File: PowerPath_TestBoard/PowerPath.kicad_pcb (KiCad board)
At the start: 2 copper layers, 86 parts, among them J1 24V Test, J2 +24V_Ext, J3 12V Test, J4 5V Test, J5 3V Test, J6 +V_in_24V, J7 GND, J8 +Vin_5V, U1 LM76202QPWPRQ1, U2 MCP1826S_LDO, U3 LMR51635XDDCR, U4 LMR51635XDDCR

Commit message: 1st iteration layout review
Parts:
- removed TP13: V_in_24V, TestPoint:TestPoint_THTPad_D3.0mm_Drill1.5mm
- added J9: +3V3_Ext, UTSVT_Connectors:5754, F.Cu at (161.7, 71.5)
- F1: value 1A -> 5A
- JP1, JP2, JP3, JP4, JP5, JP6, JP7: footprint Connector_PinHeader_1.00mm:PinHeader_1x02_P1.00mm_Vertical -> Connector_PinHeader_2.54mm:PinHeader_1x02_P2.54mm_Vertical
- moved TP9 194.2 mm to (224.3, 77.1)
- moved J4 180.0 mm to (224.6, 102.0)
- moved TP8 163.4 mm to (215.7, 117.3)
- moved J6 159.3 mm to (224.4, 88.0)
- moved TP16 155.4 mm to (214.2, 102.2)
- moved TP15 153.9 mm to (207.1, 96.2)
- moved TP14 149.7 mm to (214.1, 96.1)
- moved TP7 148.0 mm to (207.1, 101.9)
- moved J8 147.1 mm to (224.5, 114.7)
- moved R7 143.2 mm to (213.8, 110.6), turned to -90 degrees
- moved R18 136.2 mm to (182.1, 96.5), turned to 90 degrees
- moved TP3 134.9 mm to (179.1, 69.2)
- moved C14 133.1 mm to (197.5, 97.5)
- moved R8 132.2 mm to (197.2, 113.6), turned to -90 degrees
- moved R19 131.9 mm to (185.1, 96.5), turned to -90 degrees
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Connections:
- net +24V_Ext renamed /+24V_Ext
- net +Vin_5V renamed /+Vin_5V
- net Net-(J2-Pin_1) renamed /+24V_Ext_In
- C12 pad 1: +V_in_24V -> /+V_in_24V
- C8 pad 1: /12VBuck/V_in_24V -> /+V_in_24V
- J6 pad 1: +V_in_24V -> /+V_in_24V
- JP5 pad 2: /12VBuck/V_in_24V -> /+V_in_24V
- JP6 pad 2: +V_in_24V -> /+V_in_24V
- R3 pad 1: /12VBuck/V_in_24V -> /+V_in_24V
- R4 pad 1: +V_in_24V -> /+V_in_24V
- TP9 pad 1: /12VBuck/V_in_24V -> /+V_in_24V
- U3 pad 2: /12VBuck/V_in_24V -> /+V_in_24V
- U3 pad 3: /12VBuck/V_in_24V -> /+V_in_24V
- U4 pad 2: +V_in_24V -> /+V_in_24V
- U4 pad 3: +V_in_24V -> /+V_in_24V
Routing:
- net Net-(D7-A): track 0.00 -> 77.5 mm, vias 0 -> 2
- net Net-(D2-A): track 0.00 -> 68.1 mm, vias 0 -> 2
- net Net-(D8-A): track 0.00 -> 67.9 mm, vias 0 -> 2
- net Net-(D6-A): track 0.00 -> 60.1 mm, vias 0 -> 2
- net Net-(D4-A): track 0.00 -> 48.5 mm, vias 0 -> 2
- net Net-(D3-A): track 0.00 -> 48.5 mm, vias 0 -> 2
- net /+V_in_24V: track 0.00 -> 46.6 mm
- net /12VBuck/FB: track 0.00 -> 41.2 mm
- net /5VBuck/SW: track 0.00 -> 37.3 mm, vias 0 -> 1
- net Net-(D1-A): track 0.00 -> 35.5 mm, vias 0 -> 2
- net /5VBuck/CB: track 0.00 -> 27.5 mm, vias 0 -> 1
- net /Fault_TP: track 0.00 -> 26.9 mm
- net Net-(D5-A): track 0.00 -> 25.3 mm, vias 0 -> 2
- net /V_out_12V: track 0.00 -> 25.3 mm
- net /5VBuck/FB: track 0.00 -> 22.9 mm
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- added copper zone on F.Cu, net /+24V_Ext
- added copper zone on F.Cu, net /+24V_Ext_In
- added copper zone on F.Cu, net /+V_in_24V
- added copper zone on F.Cu, net /+V_out_5V_Buck
- added copper zone on F.Cu, net /+Vin_5V
- added copper zone on F.Cu, net /+Vout_3V3
- added copper zone on F.Cu, net /24V_OUT
- added copper zone on F.Cu, net /PowerProtection/RTN
- added copper zone on F.Cu, net /V_out_12V
- added copper zone on B.Cu, net GND
- added copper zone on F.Cu, net GND
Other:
- board outline added: 95.5 x 62.9 mm
- board text added: "+24V Ext"
- board text added: "+3V3 Ext"
- board text added: "+5V Ext"
- board text added: "12V Buck TP"
- board text added: "5V Buck TP"
- board text added: "5V Vout"
- board text added: "CB"
- board text added: "FB"
- board text added: "PP-12V"
- board text added: "PP-5V"
- board text added: "Power Path Test Board"
- board text added: "SW"
- board text removed: "+24V PP"
- board text removed: "+5V"
- board text removed: "12V Buck CB"
- board text removed: "12V Buck FB"
- board text removed: "12V Buck SW"
- board text removed: "5V Buck CB"
- board text removed: "5V Buck FB"
- board text removed: "5V Buck SW"
- board text removed: "PP-12V Buck"
- board text removed: "PP-5V Buck"
- board text removed: "U3"
- board text removed: "U4"
- board text removed: "Vin_24V"
- board text removed: "Vout 5V"

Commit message: addressed all final comments, review?
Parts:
- removed the C1 at (165.6, 79.9)
- removed the C2 at (168.5, 80.2)
- removed the D9 at (162.4, 87.3)
- removed the J9 at (161.7, 71.5)
- removed the R16 at (184.4, 84.1)
- removed the R17 at (167.9, 89.9)
- removed the TP2 at (171.8, 69.0)
- removed the TP3 at (179.1, 69.2)
- removed the U1 at (174.7, 82.8)
- added C6: 10n, Capacitor_SMD:C_0603_1608Metric_Pad1.08x0.95mm_HandSolder, F.Cu at (171.5, 77.5)
- added C7: 10u, Capacitor_SMD:C_0805_2012Metric_Pad1.18x1.45mm_HandSolder, F.Cu at (182.5, 79.5)
- added G***: LHRs_LOGO, UTSVT_Logos:LHRs_LOGO, F.Cu at (224.5, 74.2)
- added G***: LOGO, LOGO, B.Cu at (224.3, 74.2)
- added H1: MountingHole, MountingHole:MountingHole_3mm_Pad_TopBottom, F.Cu at (139.8, 67.2)
- added H2: MountingHole, MountingHole:MountingHole_3mm_Pad_TopBottom, F.Cu at (235.1, 67.2)
- added H3: MountingHole, MountingHole:MountingHole_3mm_Pad_TopBottom, F.Cu at (235.1, 120.0)
- added H4: MountingHole, MountingHole:MountingHole_3mm_Pad_TopBottom, F.Cu at (139.8, 120.0)
- added IC1: LM74502DDFR, UTSVT_Power:SOT65P280X110-8N, F.Cu at (177.4, 82.3)
- added Q1: PSMN012-100YS, PSMN012-100YS:TO127P600X120-5N, F.Cu at (169.1, 84.2)
- added Q2: PSMN012-100YS, PSMN012-100YS:TO127P600X120-5N, F.Cu at (178.1, 86.8)
- added TP14: 24V_OUT, TestPoint:TestPoint_THTPad_D3.0mm_Drill1.5mm, F.Cu at (171.2, 66.6)
- added TP15: 24V_OUT, TestPoint:TestPoint_THTPad_D3.0mm_Drill1.5mm, F.Cu at (164.4, 66.6)
- added TP16: 24V_OUT, TestPoint:TestPoint_THTPad_D3.0mm_Drill1.5mm, F.Cu at (181.3, 71.2)
- added TP17: 24V_OUT, TestPoint:TestPoint_THTPad_D3.0mm_Drill1.5mm, F.Cu at (167.7, 71.2)
- added TP18: 24V_OUT, TestPoint:TestPoint_THTPad_D3.0mm_Drill1.5mm, F.Cu at (161.1, 71.2)
- added TP19: 24V_OUT, TestPoint:TestPoint_THTPad_D3.0mm_Drill1.5mm, F.Cu at (177.2, 66.6)
- C3: value 100nF -> 0.1u
- C4: value 1uF -> 1u
- C5: value 10uF -> 220n; footprint Capacitor_SMD:C_0805_2012Metric_Pad1.18x1.45mm_HandSolder -> Capacitor_SMD:C_0603_1608Metric_Pad1.08x0.95mm_HandSolder
- D10: value TVS -> SMAF4758A; footprint Diode_SMD:D_SOD-123F -> UTSVT_Passives:SODFL5026X125N
- F1: footprint UTSVT_Connectors:FUSE_3568 -> UTSVT_Power:Fuse-3557-2
- R10: value 590 -> 1k
- R11: value 2.1k -> 33
- R12: value 10k -> 223k
- R13: value 402k -> 137k
- R14: value 24m -> 10k
- R9: value 45.3k -> 10k
- TP_3.3V1: footprint TestPoint:TestPoint_Loop_D1.80mm_Drill1.0mm_Beaded -> TestPoint:TestPoint_THTPad_D3.0mm_Drill1.5mm
- moved TP4 63.1 mm to (187.2, 66.6)
- moved C3 21.7 mm to (162.4, 87.0)
- moved R15 19.6 mm to (165.0, 75.0), turned to 180 degrees
- moved TP1 17.6 mm to (157.3, 66.6)
- moved R12 17.6 mm to (165.9, 79.6), turned to 90 degrees
- moved R14 13.8 mm to (164.3, 87.1), turned to 90 degrees
- moved TP7 13.2 mm to (213.6, 84.8)
- moved R13 13.1 mm to (164.0, 79.7), turned to -90 degrees
- moved C5 12.9 mm to (174.4, 78.6), turned to 0 degrees
- moved D10 12.3 mm to (174.1, 74.4), turned to 90 degrees
- moved TP2 9.62 mm to (187.7, 71.2)
- moved R11 8.94 mm to (173.9, 81.0), turned to 90 degrees
- moved R10 8.63 mm to (169.8, 79.6), turned to -90 degrees
- moved R9 7.42 mm to (167.7, 79.7)
- moved C4 5.87 mm to (176.9, 75.6), turned to -90 degrees
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- renumbered C6 to C1, C7 to C2, D11 to D9, J3 to J4, J4 to J5, J5 to J6, J6 to J7, J7 to J8, J8 to J9, R18 to R16, R19 to R17, R20 to R18, R21 to R19, TP12 to TP10, TP14 to TP11, TP15 to TP12, TP16 to TP13, TP4 to TP2, TP5 to TP3, TP6 to TP4, TP7 to TP5, TP8 to TP6, TP9 to TP7, TP10 to TP8, TP11 to TP9, U2 to U1, U3 to U2, U4 to U3
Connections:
- net /PowerProtection/OVP renamed /PowerProtection/gate
- C3 pad 1: Net-(U1-DVDT) -> /+24V_Ext
- C3 pad 2: /PowerProtection/RTN -> GND
- C4 pad 1: /24V_OUT -> GND
- C4 pad 2: GND -> Net-(D10-K)
- C5 pad 1: /24V_OUT -> Net-(D10-K)
- C5 pad 2: GND -> Net-(IC1-VCAP)
- D10 pad 1: /IMON_TP -> Net-(D10-K)
- JP1 pad 2: /24V_OUT -> /Vout_24V
- JP5 pad 1: /24V_OUT -> /Vout_24V
- JP6 pad 1: /24V_OUT -> /Vout_24V
- R10 pad 1: /PowerProtection/UVLO -> Net-(C6-Pad1)
- R11 pad 2: /PowerProtection/RTN -> Net-(IC1-GATE)
- R12 pad 1: /PowerProtection/ILIM -> /+24V_Ext
- R12 pad 2: /PowerProtection/RTN -> Net-(IC1-OV)
- R13 pad 1: /PowerProtection/MODE -> Net-(IC1-EN/UVLO)
- R13 pad 2: /PowerProtection/RTN -> /+24V_Ext
- R14 pad 1: /PowerProtection/IMON -> GND
- R14 pad 2: /PowerProtection/RTN -> /+24V_Ext
- R15 pad 1: /24V_OUT -> Net-(IC1-OV)
- R15 pad 2: /Fault_TP -> GND
- R2 pad 1: /24V_OUT -> /Vout_24V
- R9 pad 1: /+24V_Ext -> Net-(D10-K)
- R9 pad 2: /PowerProtection/UVLO -> /+24V_Ext
- TP2 pad 1: /24V_OUT -> /Vout_24V
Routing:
- net Net-(D10-K): track 0.00 -> 27.6 mm
- net /Fault_TP: track 26.9 -> 0.00 mm
- net Net-(IC1-EN/UVLO): track 0.00 -> 26.7 mm, vias 0 -> 2
- net /PowerProtection/gate: track 10.7 -> 36.7 mm, vias 0 -> 2
- net +3.3V: track 21.1 -> 0.00 mm, vias 2 -> 0
- net /IMON_TP: track 20.6 -> 0.00 mm, vias 1 -> 0
- net Net-(IC1-OV): track 0.00 -> 20.5 mm
- net Net-(IC1-VCAP): track 0.00 -> 19.5 mm
- net /PowerProtection/source: track 0.00 -> 16.3 mm, vias 0 -> 1
- net /PowerProtection/IMON: track 12.2 -> 0.00 mm, vias 2 -> 0
- net /PowerProtection/UVLO: track 11.9 -> 0.00 mm
- net /+24V_Ext: track 5.13 -> 15.6 mm
- net /24V_OUT: track 9.74 -> 0.00 mm
- net Net-(U1-DVDT): track 9.12 -> 0.00 mm
- net /PowerProtection/ILIM: track 8.72 -> 0.00 mm
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- added copper zone on F.Cu, net /PowerProtection/source
- added copper zone on F.Cu, net /Vout_24V
- removed copper zone on F.Cu, net /24V_OUT
- removed copper zone on F.Cu, net /PowerProtection/RTN
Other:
- board size 95.5 x 62.9 mm -> 105.4 x 62.9 mm
- board text added: "12V"
- board text added: "12V Vout"
- board text added: "24V"
- board text added: "24V 12Buck"
- board text added: "24V 5Buck"
- board text added: "24V Ext"
- board text added: "24V PP"
- board text added: "3V3 LDO"
- board text added: "5/29/2026"
- board text added: "5V"
- board text added: "5V LDO"
- board text added: "EN"
- board text added: "Gate"
- board text added: "OV"
- board text added: "Shuopu Wang"
- board text added: "Source"
- board text added: "VCAP"
- board text added: "VS"
- board text added: "Vout 24V"
- board text removed: "+3V3 Ext"
- board text removed: "24V Out"
- board text removed: "PP Fault"
- board text removed: "PP IMON"
- board text removed: "Vout 12V"

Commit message: finished tony's review, should be good?
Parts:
- removed H4: MountingHole, MountingHole:MountingHole_3mm_Pad_TopBottom
- added G***: LOGO, LOGO, F.Cu at (143.2, 100.8)
- added H5: MountingHole_Pad_MP, MountingHole:MountingHole_3mm_Pad_TopBottom, F.Cu at (235.1, 120.0)
- added TP20: GND, TestPoint:TestPoint_THTPad_D3.0mm_Drill1.5mm, F.Cu at (161.2, 121.5)
- added TP21: GND, TestPoint:TestPoint_THTPad_D3.0mm_Drill1.5mm, F.Cu at (211.1, 121.4)
- H1, H2, H3: value MountingHole -> MountingHole_Pad_MP
- moved H2 108.9 mm to (139.8, 120.0), turned to 0 degrees
- moved D7 68.8 mm to (214.5, 112.8), turned to 180 degrees
- moved D6 58.3 mm to (203.4, 102.0), turned to -90 degrees
- moved D8 52.8 mm to (198.6, 116.4), turned to 180 degrees
- moved H3 52.8 mm to (235.1, 67.2)
- moved D2 49.0 mm to (192.6, 79.0), turned to 180 degrees
- moved D4 42.2 mm to (184.6, 89.6), turned to -90 degrees
- moved D3 37.8 mm to (182.8, 89.6), turned to -90 degrees
- moved D5 23.5 mm to (169.4, 103.4)
- moved D1 21.0 mm to (161.4, 76.2), turned to 0 degrees
- moved TP9 2.75 mm to (155.1, 106.3)
- moved TP3 1.75 mm to (155.1, 113.2)
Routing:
- net Net-(D7-A): track 77.5 -> 1.47 mm, vias 2 -> 0
- net Net-(D2-A): track 68.2 -> 1.68 mm, vias 2 -> 0
- net Net-(D8-A): track 67.9 -> 2.22 mm, vias 2 -> 0
- net Net-(D6-A): track 60.1 -> 2.12 mm, vias 2 -> 0
- net Net-(D4-A): track 48.5 -> 1.75 mm, vias 2 -> 0
- net Net-(D3-A): track 48.5 -> 2.14 mm, vias 2 -> 0
- net Net-(D1-A): track 34.1 -> 2.78 mm, vias 2 -> 0
- net Net-(D5-A): track 25.7 -> 1.61 mm, vias 2 -> 0
- net /+V_out_5V_Buck: track 13.3 -> 10.2 mm
- net Net-(J1-Pin_1): track 16.9 -> 14.0 mm
- net /12VBuck/FB: track 35.1 -> 32.6 mm
- net Net-(J6-Pin_1): track 9.97 -> 7.85 mm
- net GND: track 2.41 -> 4.46 mm, vias 43 -> 87
- net /+Vin_5V: track 22.9 -> 21.0 mm
- net /V_out_12V: track 23.9 -> 22.3 mm
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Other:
- board text added: "5/30/2026"
- board text removed: "5/29/2026"

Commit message: ready for lil shah
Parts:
- moved TP18 20.3 mm to (181.4, 71.3)
- moved TP16 20.2 mm to (161.1, 71.1)
- moved R13 17.5 mm to (181.4, 77.6), turned to 90 degrees
- moved R15 7.81 mm to (172.8, 74.9)
- moved R12 7.37 mm to (172.8, 77.0), turned to 0 degrees
- moved R9 2.90 mm to (164.8, 79.6)
- moved C5 2.85 mm to (177.1, 79.4)
- moved C6 2.67 mm to (169.1, 78.7), turned to 180 degrees
- moved R11 2.54 mm to (172.8, 78.7), turned to 0 degrees
- moved D10 2.40 mm to (176.4, 75.1)
- moved C4 2.21 mm to (178.9, 76.5)
- moved R10 1.43 mm to (170.9, 80.5), turned to 0 degrees
- moved C7 0.70 mm to (183.2, 79.5)
- moved TP15 0.26 mm to (164.7, 66.6)
- moved IC1 0.25 mm to (177.2, 82.3)
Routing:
- net /+24V_Ext: track 15.6 -> 32.4 mm, vias 0 -> 2
- net Net-(IC1-EN/UVLO): track 26.7 -> 14.9 mm, vias 2 -> 0
- net /PowerProtection/gate: track 36.8 -> 30.3 mm, vias 2 -> 3
- net /PowerProtection/source: track 16.6 -> 21.4 mm
- net Net-(D10-K): track 27.8 -> 31.5 mm, vias 1 -> 2
- net Net-(IC1-OV): track 20.5 -> 17.8 mm
- net Net-(IC1-VCAP): track 18.7 -> 17.2 mm, vias 1 -> 0
- net Net-(IC1-GATE): track 3.54 -> 4.65 mm
- net GND: track 4.46 -> 4.61 mm, vias 87 -> 101

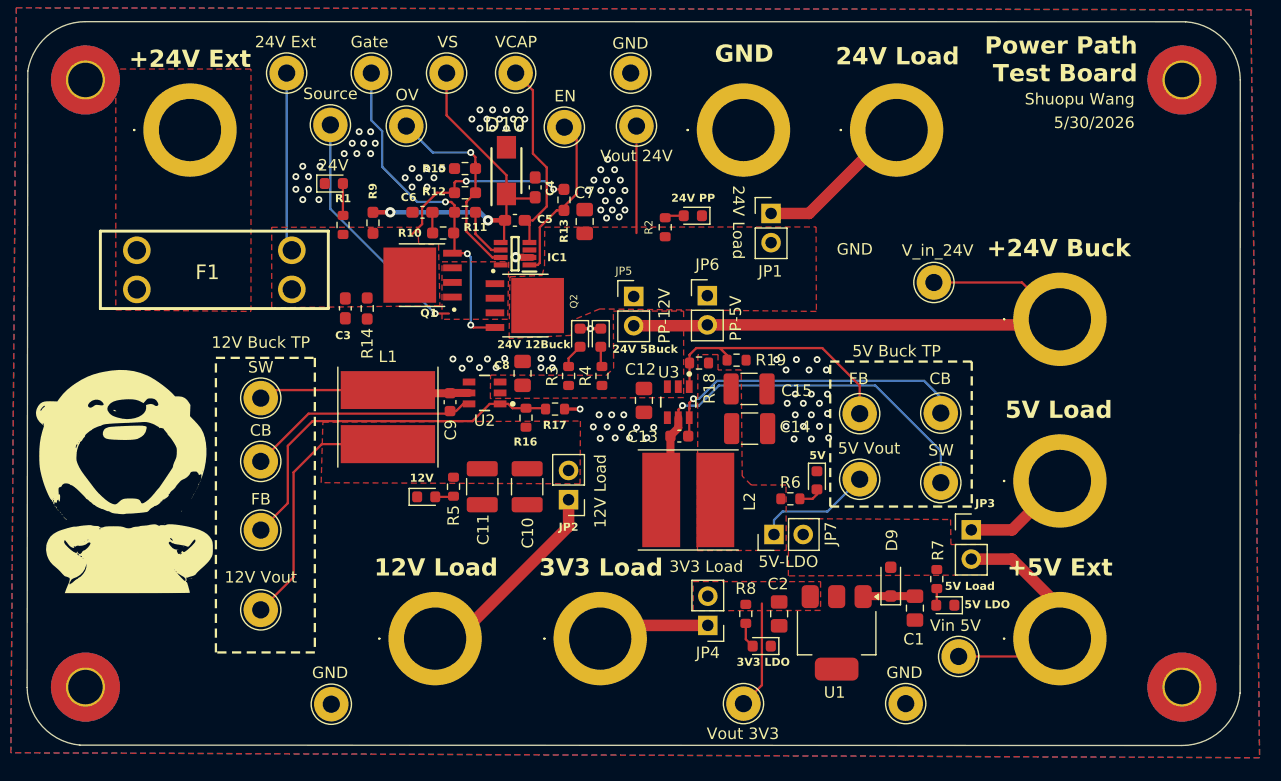
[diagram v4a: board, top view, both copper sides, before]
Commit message: added shorting jumpers
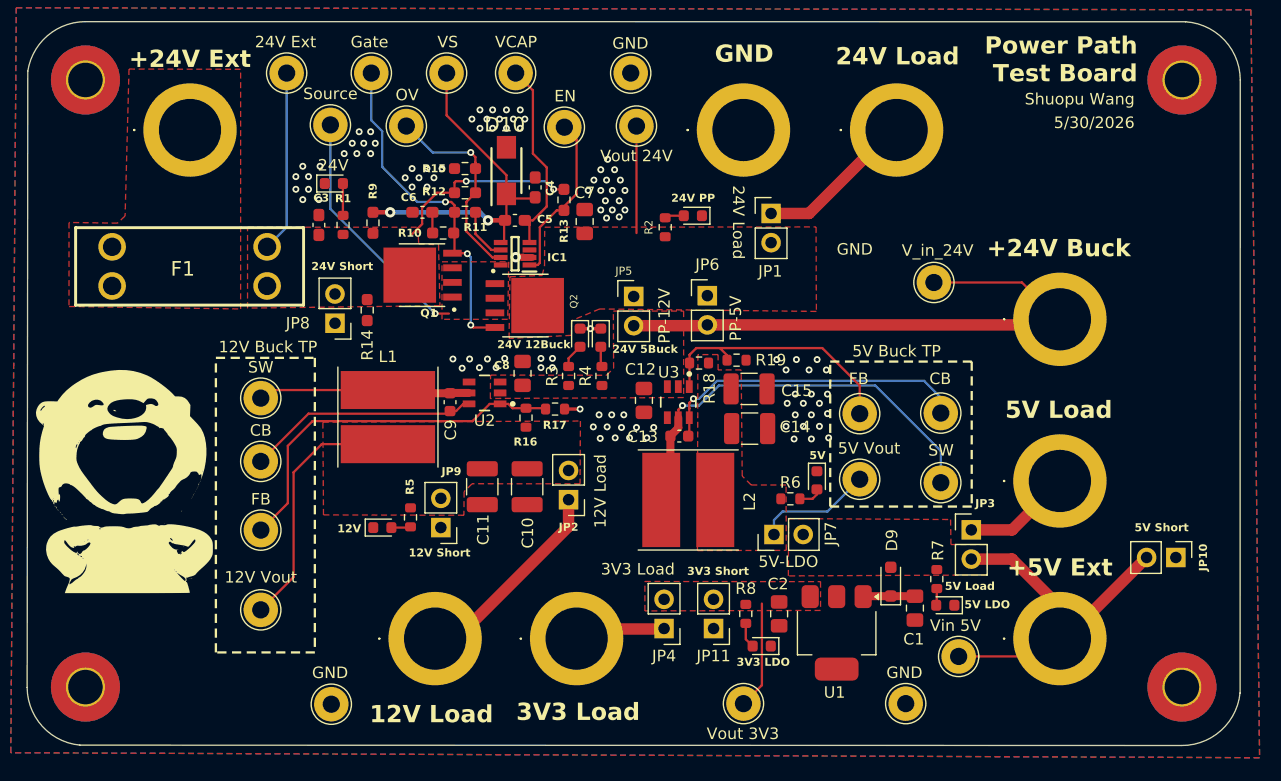
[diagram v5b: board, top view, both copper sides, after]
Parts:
- added JP10: 12V Load, Connector_PinHeader_2.54mm:PinHeader_1x02_P2.54mm_Vertical, F.Cu at (234.6, 108.7)
- added JP11: 12V Load, Connector_PinHeader_2.54mm:PinHeader_1x02_P2.54mm_Vertical, F.Cu at (194.4, 114.9)
- added JP8: 12V Load, Connector_PinHeader_2.54mm:PinHeader_1x02_P2.54mm_Vertical, F.Cu at (161.5, 88.3)
- added JP9: 12V Short, Connector_PinHeader_2.54mm:PinHeader_1x02_P2.54mm_Vertical, F.Cu at (170.7, 106.1)
- moved C3 7.61 mm to (160.1, 79.8), turned to 90 degrees
- moved D5 4.66 mm to (165.6, 106.1)
- moved R5 4.59 mm to (168.1, 105.2)
- moved JP4 3.81 mm to (190.1, 114.9)
- moved F1 2.17 mm to (148.9, 83.4)
- moved J6 2.05 mm to (182.5, 115.8)
- moved R14 0.14 mm to (164.3, 87.2)
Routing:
- net /+Vin_5V: track 21.0 -> 31.4 mm
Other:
- board text added: "12V Short"
- board text added: "24V Short"
- board text added: "3V3 Short"
- board text added: "5V Short"

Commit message: updated with PP + gen gebers
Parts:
- removed the R15 at (172.8, 74.9)
- removed the TP14 at (171.2, 66.6)
- removed the TP15 at (164.7, 66.6)
- removed the TP16 at (161.1, 71.1)
- removed the TP17 at (167.7, 71.2)
- removed the TP18 at (181.4, 71.3)
- added D11: SMAF4758A, UTSVT_Passives:SODFL5026X125N, F.Cu at (176.4, 75.7)
- added TP2: 24V_OUT, TestPoint:TestPoint_THTPad_D3.0mm_Drill1.5mm, F.Cu at (164.6, 66.6)
- added TP20: +V_out_5V, TestPoint:TestPoint_THTPad_D3.0mm_Drill1.5mm, F.Cu at (177.1, 66.6)
- added TP21: +V_out_5V, TestPoint:TestPoint_THTPad_D3.0mm_Drill1.5mm, F.Cu at (167.9, 71.2)
- added TP22: +V_out_5V, TestPoint:TestPoint_THTPad_D3.0mm_Drill1.5mm, F.Cu at (181.5, 71.3)
- added TP3: 24V_OUT, TestPoint:TestPoint_THTPad_D3.0mm_Drill1.5mm, F.Cu at (161.1, 71.2)
- added TP6: GND, TestPoint:TestPoint_THTPad_D3.0mm_Drill1.5mm, F.Cu at (206.6, 84.7)
- C7: footprint Capacitor_SMD:C_0805_2012Metric_Pad1.18x1.45mm_HandSolder -> Capacitor_SMD:C_0603_1608Metric_Pad1.08x0.95mm_HandSolder
- D10: value SMAF4758A -> SMBJ30CD; footprint UTSVT_Passives:SODFL5026X125N -> SMBJ30CD:DIONM5436X244N
- G***: moved to F.Cu
- IC1: footprint UTSVT_Power:SOT65P280X110-8N -> UTSVT_Power:LM74502DDFR
- JP9: value 12V Short -> 12V Load
- Q1, Q2: footprint PSMN012-100YS:TO127P600X120-5N -> UTSVT_Power:PSMN012-100YS
- R10: value 1k -> 33
- R11: value 33 -> 221k
- R12: value 223k -> 137k
- R13: value 137k -> 10k
- TP19: value 24V_OUT -> +V_out_5V
- moved R14 21.2 mm to (182.2, 75.7), turned to 0 degrees
- moved G*** 17.5 mm to (234.8, 88.2), turned to 0 degrees
- moved D10 14.2 mm to (162.6, 78.6)
- moved R13 9.85 mm to (171.6, 76.6), turned to -90 degrees
- moved R12 8.60 mm to (181.3, 78.2), turned to 90 degrees
- moved TP19 5.98 mm to (171.2, 66.5)
- moved D1 5.90 mm to (167.3, 75.7), turned to 180 degrees
- moved R1 5.74 mm to (167.3, 77.2), turned to 180 degrees
- moved R11 3.52 mm to (169.9, 76.7), turned to 90 degrees
- moved TP7 3.01 mm to (184.2, 66.4)
- moved C6 2.62 mm to (170.9, 80.6)
- moved R10 2.33 mm to (172.7, 79.1)
- moved R9 2.23 mm to (167.0, 79.6)
- moved G*** 1.90 mm to (143.3, 102.7)
- moved G*** 1.36 mm to (224.3, 75.5)
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- renumbered H5 to H1, H1 to H2, H2 to H3, H3 to H4, J4 to J3, J5 to J4, J6 to J5, J7 to J6, J8 to J7, J9 to J8, JP7 to JP11, JP8 to JP7, JP11 to JP8, R16 to R15, R17 to R16, R18 to R17, R19 to R18, TP5 to TP10, TP6 to TP11, TP7 to TP12, TP8 to TP13, TP9 to TP14, TP10 to TP15, TP11 to TP16, TP12 to TP17, TP13 to TP18, TP2 to TP4, TP3 to TP5, TP4 to TP7, TP20 to TP8, TP21 to TP9
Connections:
- C4 pad 2: Net-(D10-K) -> Net-(D11-K)
- C5 pad 1: Net-(D10-K) -> Net-(D11-K)
- C6 pad 1: Net-(C6-Pad1) -> /PowerProtection/gate
- D10 pad 1: Net-(D10-K) -> /+24V_Ext
- IC1 pad 5: Net-(D10-K) -> Net-(D11-K)
- R10 pad 1: Net-(C6-Pad1) -> /PowerProtection/gate
- R10 pad 2: /PowerProtection/gate -> Net-(IC1-GATE)
- R11 pad 1: /PowerProtection/gate -> /+24V_Ext
- R11 pad 2: Net-(IC1-GATE) -> Net-(IC1-OV)
- R12 pad 1: /+24V_Ext -> Net-(IC1-EN/UVLO)
- R12 pad 2: Net-(IC1-OV) -> /+24V_Ext
- R13 pad 1: Net-(IC1-EN/UVLO) -> Net-(IC1-OV)
- R13 pad 2: /+24V_Ext -> GND
- R14 pad 1: GND -> Net-(IC1-EN/UVLO)
- R14 pad 2: /+24V_Ext -> GND
- R9 pad 1: Net-(D10-K) -> Net-(D11-K)
- TP19 pad 1: Net-(IC1-VCAP) -> Net-(D11-K)
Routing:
- net Net-(D10-K): track 31.5 -> 0.00 mm, vias 2 -> 0
- net Net-(D11-K): track 0.00 -> 29.5 mm, vias 0 -> 2
- net /PowerProtection/gate: track 30.3 -> 33.0 mm, vias 3 -> 2
- net GND: track 4.61 -> 6.52 mm, vias 101 -> 100
- net /+24V_Ext: track 32.6 -> 34.4 mm
- net Net-(C6-Pad1): track 1.81 -> 0.00 mm
- net /Vout_24V: track 7.70 -> 9.51 mm
- net Net-(IC1-OV): track 17.8 -> 16.7 mm
- net Net-(D1-A): track 2.78 -> 1.65 mm
- net Net-(IC1-VCAP): track 17.2 -> 16.5 mm
- net Net-(IC1-EN/UVLO): track 14.9 -> 15.5 mm
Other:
- board text added: "24V In"
- board text added: "24V Out"
- board text added: "24V-12V Buck"
- board text added: "24V-5V Buck"
- board text added: "LDO"
- board text added: "Max 5A"
- board text added: "PP Block"
- board text added: "PP TP"
- board text added: "Rev X 2026"
- board text removed: "24V"
- board text removed: "24V Ext"
- board text removed: "Vout 24V"

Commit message: JLC gebers + minor silk fixes
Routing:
- net GND: track 6.52 -> 9.29 mm, vias 100 -> 102
